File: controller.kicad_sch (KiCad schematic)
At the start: 19 parts, among them U4 STM32H742VGTx

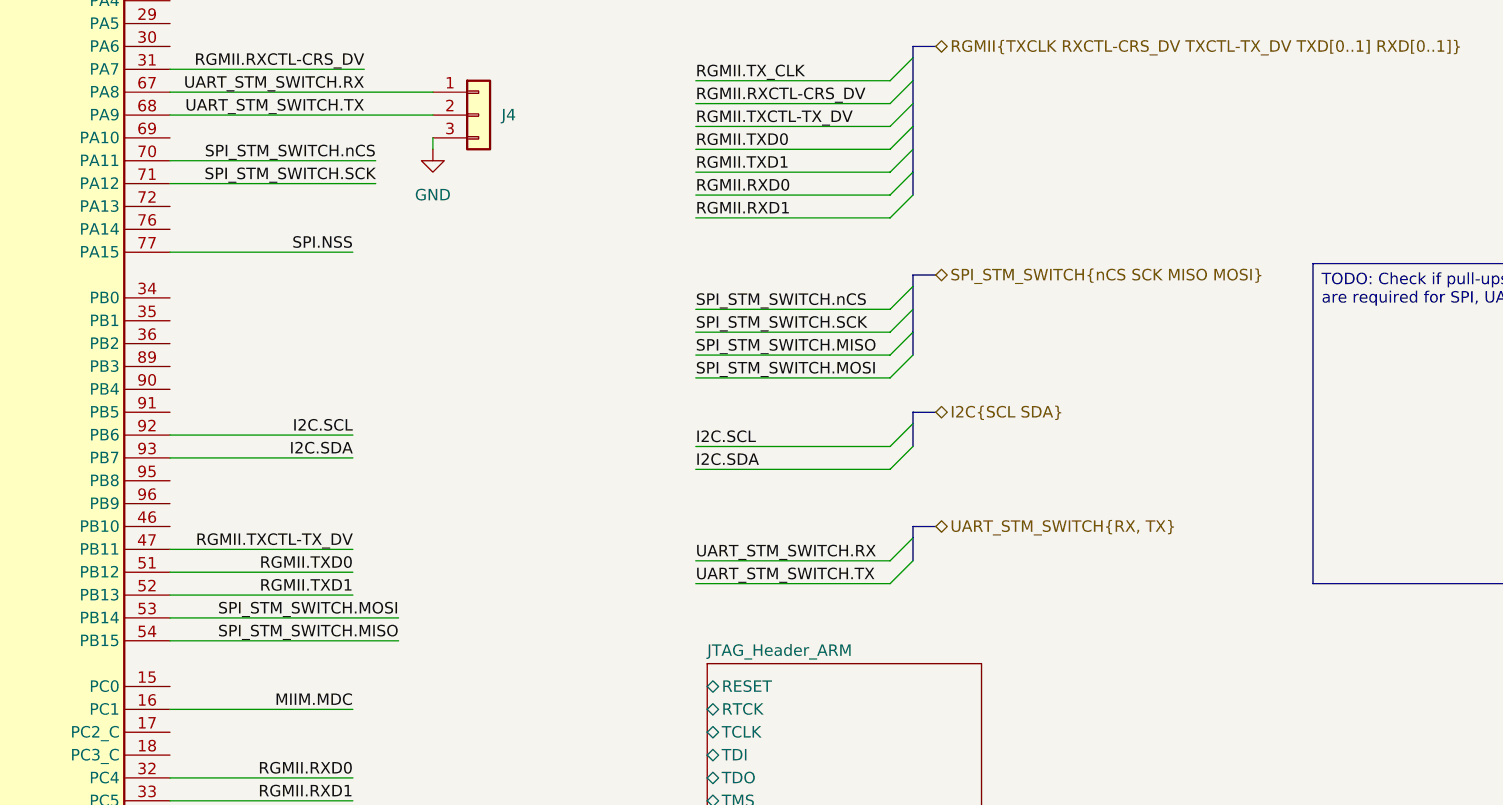
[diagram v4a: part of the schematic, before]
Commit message: connects SPI from STM to Switch. Refs: #1
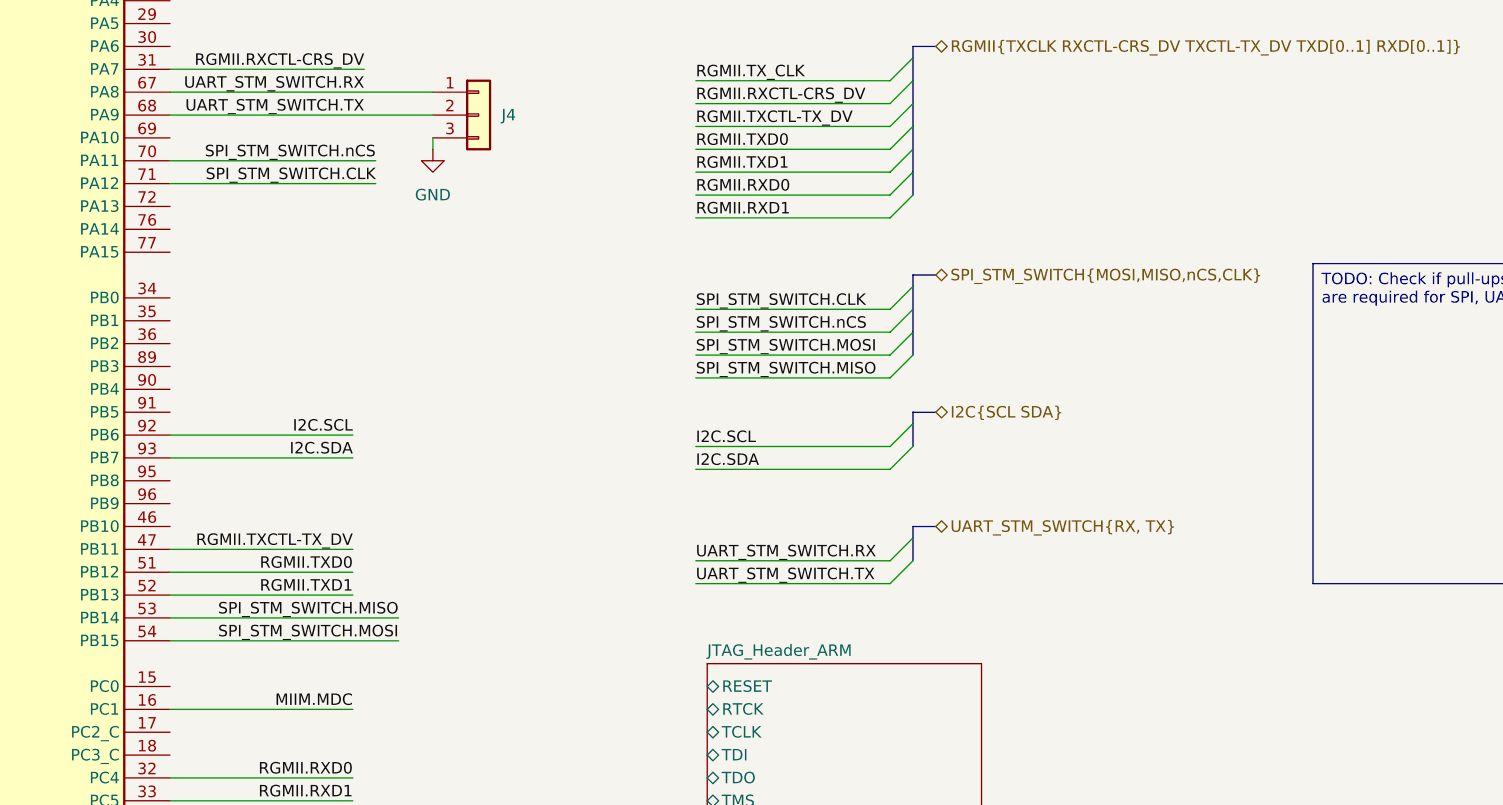
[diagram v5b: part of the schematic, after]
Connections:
- net SPI_STM_SWITCH.MISO: now also U4.53 (PB14); no longer U4.54 (PB15)
- net SPI_STM_SWITCH.MOSI: now also U4.54 (PB15); no longer U4.53 (PB14)
- net SPI.NSS: no longer names the net of U4.77 (PA15)
- net SPI_STM_SWITCH.SCK renamed SPI_STM_SWITCH.CLK
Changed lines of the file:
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@@
+	)
+	(bus_entry
+		(at 204.47 104.14)
+		(size 2.54 -2.54)
+		(stroke
+			(width 0)
+			(type default)
+		)
+	)
+	(bus_entry
+		(at 204.47 73.66)
+		(size 2.54 -2.54)
+		(stroke
+			(width 0)
+			(type default)
+		)
+	)
+	(bus_entry
+		(at 204.47 78.74)
+		(size 2.54 -2.54)
+		(stroke
+			(width 0)
+			(type default)
+		)
+	)
+	(bus_entry
+		(at 207.01 114.3)
+		(size -2.54 2.54)
+		(stroke
+			(width 0)
+			(type default)
+		)
+	)
+	(bus_entry
+		(at 207.01 116.84)
+		(size -2.54 2.54)
+		(stroke
+			(width 0)
+			(type default)
+		)
+	)
+	(bus_entry
+		(at 204.47 71.12)
+		(size 2.54 -2.54)
+		(stroke
+			(width 0)
+			(type default)
+		)
+	)
+	(bus_entry
+		(at 207.01 88.9)
+		(size -2.54 2.54)
+		(stroke
+			(width 0)
+			(type default)
+		)
+	)
+	(bus_entry
+		(at 204.47 106.68)
+		(size 2.54 -2.54)
+		(stroke
+			(width 0)
+			(type default)
+		)
 	)
 	(bus_entry
@@
 	)
 	(bus_entry
-		(at 204.47 104.14)
-		(size 2.54 -2.54)
-		(stroke
-			(width 0)
-			(type default)
-		)
-	)
-	(bus_entry
-		(at 204.47 73.66)
-		(size 2.54 -2.54)
-		(stroke
-			(width 0)
-			(type default)
-		)
-	)
-	(bus_entry
-		(at 204.47 78.74)
-		(size 2.54 -2.54)
-		(stroke
-			(width 0)
-			(type default)
-		)
-	)
-	(bus_entry
-		(at 207.01 114.3)
-		(size -2.54 2.54)
-		(stroke
-			(width 0)
-			(type default)
-		)
-	)
-	(bus_entry
-		(at 207.01 116.84)
-		(size -2.54 2.54)
-		(stroke
-			(width 0)
-			(type default)
-		)
-	)
-	(bus_entry
-		(at 207.01 88.9)
-		(size -2.54 2.54)
-		(stroke
-			(width 0)
-			(type default)
-		)
-	)
-	(bus_entry
-		(at 204.47 71.12)
-		(size 2.54 -2.54)
-		(stroke
-			(width 0)
-			(type default)
-		)
-	)
-	(bus_entry
-		(at 204.47 106.68)
-		(size 2.54 -2.54)
-		(stroke
-			(width 0)
-			(type default)
-		)
-	)
-	(bus_entry
 		(at 203.2 50.8)
 		(size 2.54 -2.54)
@@
 	)
 	(bus_entry
+		(at 207.01 91.44)
+		(size -2.54 2.54)
+		(stroke
+			(width 0)
+			(type default)
+		)
+	)
+	(bus_entry
 		(at 285.75 16.51)
 		(size 2.54 2.54)
@@
 	)
 	(bus_entry
-		(at 207.01 91.44)
-		(size -2.54 2.54)
-		(stroke
-			(width 0)
-			(type default)
-		)
-	)
-	(bus_entry
 		(at 204.47 63.5)
 		(size 2.54 -2.54)
@@
 	(wire
 		(pts
+			(xy 182.88 93.98) (xy 204.47 93.98)
+		)
+		(stroke
+			(width 0)
+			(type default)
+		)
+	)
+	(wire
+		(pts
 			(xy 45.72 157.48) (xy 45.72 162.56)
 		)
@@
 	(wire
 		(pts
+			(xy 182.88 88.9) (xy 204.47 88.9)
+		)
+		(stroke
+			(width 0)
+			(type default)
+		)
+	)
+	(wire
+		(pts
 			(xy 40.64 21.59) (xy 45.72 21.59)
 		)
@@
 		)
 	)
+	(wire
+		(pts
+			(xy 182.88 91.44) (xy 204.47 91.44)
+		)
+		(stroke
+			(width 0)
+			(type default)
+		)
+	)
 	(bus
 		(pts
@@
 		)
 	)
+	(bus
+		(pts
+			(xy 207.01 86.36) (xy 207.01 88.9)
+		)
+		(stroke
+			(width 0)
+			(type default)
+		)
+	)
+	(bus
+		(pts
+			(xy 207.01 88.9) (xy 207.01 91.44)
+		)
+		(stroke
+			(width 0)
+			(type default)
+		)
+	)
+	(bus
+		(pts
+			(xy 207.01 91.44) (xy 207.01 93.98)
+		)
+		(stroke
+			(width 0)
+			(type default)
+		)
+	)
 	(wire
 		(pts
@@
 	(wire
 		(pts
-			(xy 182.88 91.44) (xy 204.47 91.44)
-		)
-		(stroke
-			(width 0)
-			(type default)
-		)
-	)
-	(wire
-		(pts
 			(xy 101.6 31.75) (xy 99.06 31.75)
 		)
@@
 		)
 	)
-	(bus
-		(pts
-			(xy 207.01 91.44) (xy 207.01 93.98)
-		)
-		(stroke
-			(width 0)
-			(type default)
-		)
-	)
 	(wire
 		(pts
@@
 		)
 	)
-	(bus
-		(pts
-			(xy 207.01 86.36) (xy 207.01 88.9)
-		)
-		(stroke
-			(width 0)
-			(type default)
-		)
-	)
 	(wire
 		(pts
@@
 		)
 	)
-	(bus
-		(pts
-			(xy 207.01 88.9) (xy 207.01 91.44)
-		)
-		(stroke
-			(width 0)
-			(type default)
-		)
-	)
 	(wire
 		(pts
@@
 	(wire
 		(pts
-			(xy 204.47 96.52) (xy 182.88 96.52)
-		)
-		(stroke
-			(width 0)
-			(type default)
-		)
-	)
-	(wire
-		(pts
 			(xy 58.42 77.47) (xy 78.74 77.47)
 		)
@@
 	(wire
 		(pts
-			(xy 182.88 93.98) (xy 204.47 93.98)
+			(xy 182.88 96.52) (xy 204.47 96.52)
 		)
 		(stroke
@@
 	(wire
 		(pts
-			(xy 124.46 82.55) (xy 144.78 82.55)
-		)
-		(stroke
-			(width 0)
-			(type default)
-		)
-	)
-	(wire
-		(pts
 			(xy 182.88 68.58) (xy 204.47 68.58)
 		)
@@
 			(width 0)
 			(type default)
-		)
-	)
-	(wire
-		(pts
-			(xy 182.88 88.9) (xy 204.47 88.9)
-		)
-		(stroke
-			(width 0)
-			(type default)
-		)
-	)
-	(label "SPI_STM_SWITCH.SCK"
-		(at 182.88 91.44 0)
-		(effects
-			(font
-				(size 1.27 1.27)
-			)
-			(justify left bottom)
 		)
 	)
@@
 	)
 	(label "SPI_STM_SWITCH.MOSI"
-		(at 182.88 96.52 0)
-		(effects
-			(font
-				(size 1.27 1.27)
-			)
-			(justify left bottom)
-		)
-	)
-	(label "SPI_STM_SWITCH.MISO"
 		(at 149.86 125.73 180)
 		(effects
@@
 		)
 	)
-	(label "SPI_STM_SWITCH.SCK"
+	(label "SPI_STM_SWITCH.CLK"
 		(at 147.32 74.93 180)
 		(effects
@@
 		)
 	)
-	(label "SPI_STM_SWITCH.MISO"
-		(at 182.88 93.98 0)
+	(label "SPI_STM_SWITCH.CLK"
+		(at 182.88 88.9 0)
 		(effects
 			(font
@@
 		)
 	)
-	(label "SPI_STM_SWITCH.nCS"
-		(at 182.88 88.9 0)
-		(effects
-			(font
-				(size 1.27 1.27)
-			)
-			(justify left bottom)
-		)
-	)
 	(label "I2C.SCL"
 		(at 182.88 104.14 0)
@@
 		)
 	)
+	(label "SPI_STM_SWITCH.MOSI"
+		(at 182.88 93.98 0)
+		(effects
+			(font
+				(size 1.27 1.27)
+			)
+			(justify left bottom)
+		)
+	)
 	(label "UART_STM_SWITCH.RX"
 		(at 182.88 116.84 0)
@@
 		)
 	)
+	(label "SPI_STM_SWITCH.nCS"
+		(at 182.88 91.44 0)
+		(effects
+			(font
+				(size 1.27 1.27)
+			)
+			(justify left bottom)
+		)
+	)
 	(label "RGMII.TX_CLK"
 		(at 182.88 63.5 0)
@@
 		)
 	)
-	(label "SPI.NSS"
-		(at 144.78 82.55 180)
-		(effects
-			(font
-				(size 1.27 1.27)
-			)
-			(justify right bottom)
+	(label "SPI_STM_SWITCH.MISO"
+		(at 182.88 96.52 0)
+		(effects
+			(font
+				(size 1.27 1.27)
+			)
+			(justify left bottom)
 		)
 	)
@@
 		)
 	)
-	(label "SPI_STM_SWITCH.MOSI"
+	(label "SPI_STM_SWITCH.MISO"
 		(at 149.86 123.19 180)
 		(effects
@@
 		)
 	)
-	(hierarchical_label "SPI_STM_SWITCH{nCS SCK MISO MOSI}"
+	(hierarchical_label "SPI_STM_SWITCH{MOSI,MISO,nCS,CLK}"
 		(shape bidirectional)
 		(at 209.55 85.09 0)

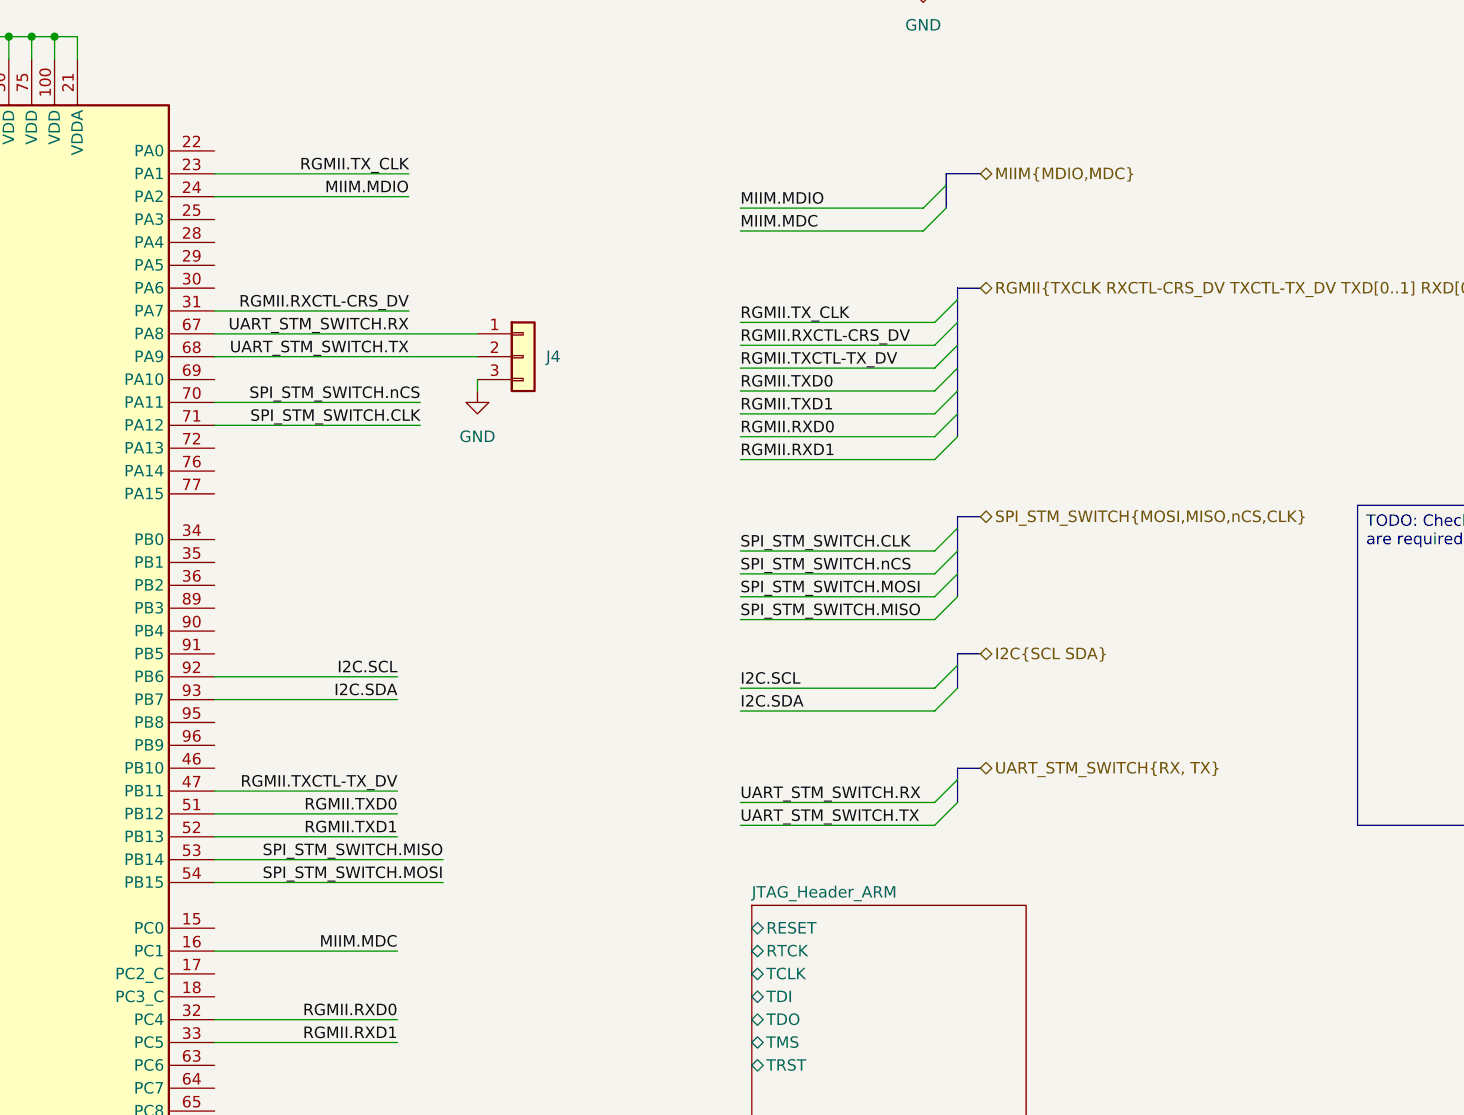
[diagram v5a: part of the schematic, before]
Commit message: connects MIIM bus from STM to Switch. Refs: #1
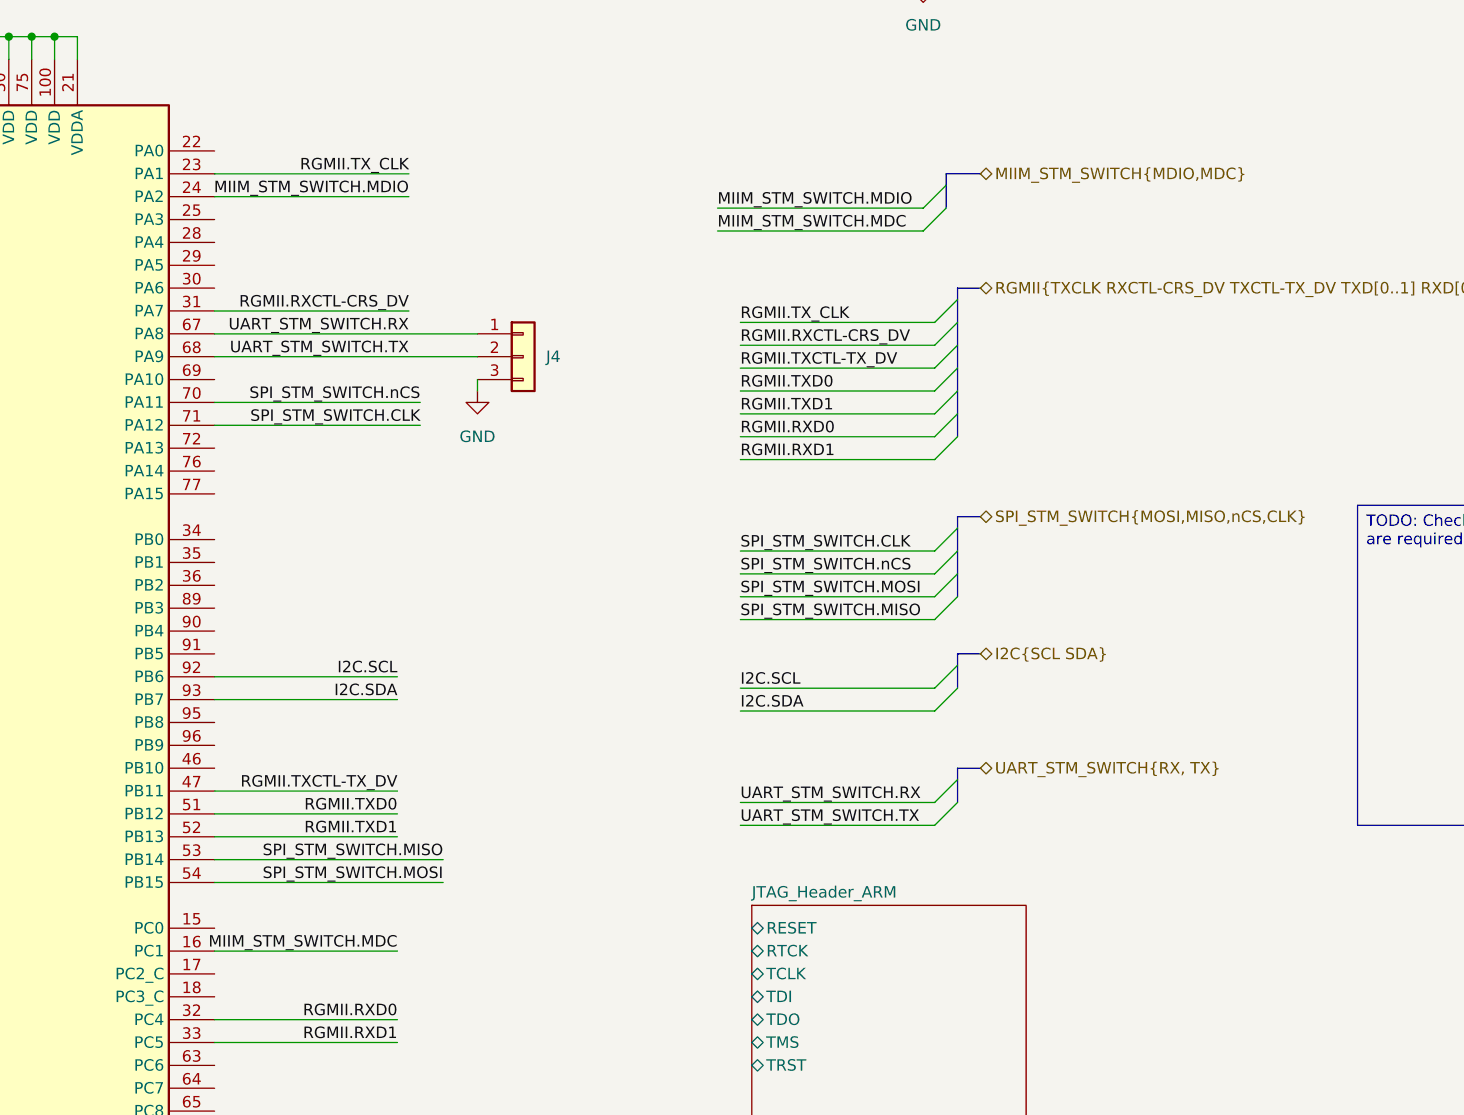
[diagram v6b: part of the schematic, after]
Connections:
- net MIIM.MDC renamed MIIM_STM_SWITCH.MDC
- net MIIM.MDIO renamed MIIM_STM_SWITCH.MDIO
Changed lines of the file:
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@@
 	(wire
 		(pts
-			(xy 182.88 50.8) (xy 203.2 50.8)
+			(xy 180.34 50.8) (xy 203.2 50.8)
 		)
 		(stroke
@@
 	(wire
 		(pts
-			(xy 182.88 53.34) (xy 203.2 53.34)
+			(xy 180.34 53.34) (xy 203.2 53.34)
 		)
 		(stroke
@@
 		)
 	)
-	(label "MIIM.MDC"
+	(label "MIIM_STM_SWITCH.MDC"
 		(at 144.78 133.35 180)
 		(effects
@@
 		)
 	)
-	(label "MIIM.MDIO"
+	(label "MIIM_STM_SWITCH.MDIO"
 		(at 146.05 49.53 180)
 		(effects
@@
 		)
 	)
-	(label "MIIM.MDC"
-		(at 182.88 53.34 0)
+	(label "MIIM_STM_SWITCH.MDC"
+		(at 180.34 53.34 0)
 		(effects
 			(font
@@
 		)
 	)
-	(label "MIIM.MDIO"
-		(at 182.88 50.8 0)
+	(label "MIIM_STM_SWITCH.MDIO"
+		(at 180.34 50.8 0)
 		(effects
 			(font
@@
 		)
 	)
-	(hierarchical_label "MIIM{MDIO,MDC}"
+	(hierarchical_label "MIIM_STM_SWITCH{MDIO,MDC}"
 		(shape bidirectional)
 		(at 209.55 46.99 0)
